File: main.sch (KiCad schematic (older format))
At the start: 27 parts, among them J4 Screw_Terminal_01x03, J5 Expansion, P1 TC2030-CTX-Tag-Connect-ESP32, U11 MAX485E, U12 TJA1051T, U13 TM8211, U2 ESP32-WROOM

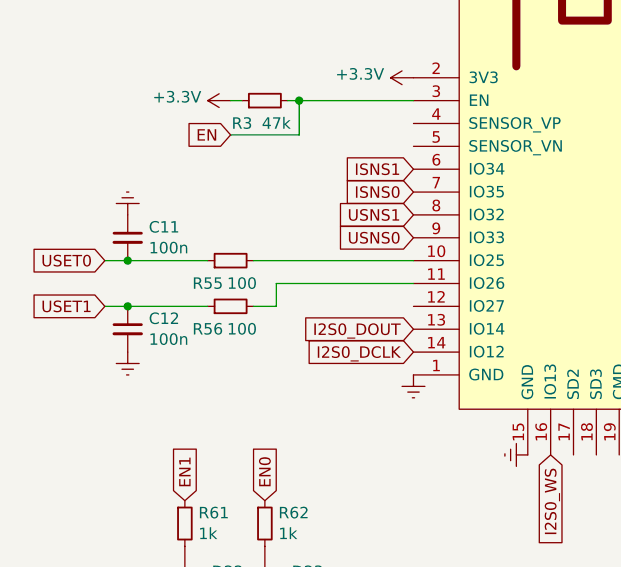
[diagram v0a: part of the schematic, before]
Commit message: modified Voltage DAC bias
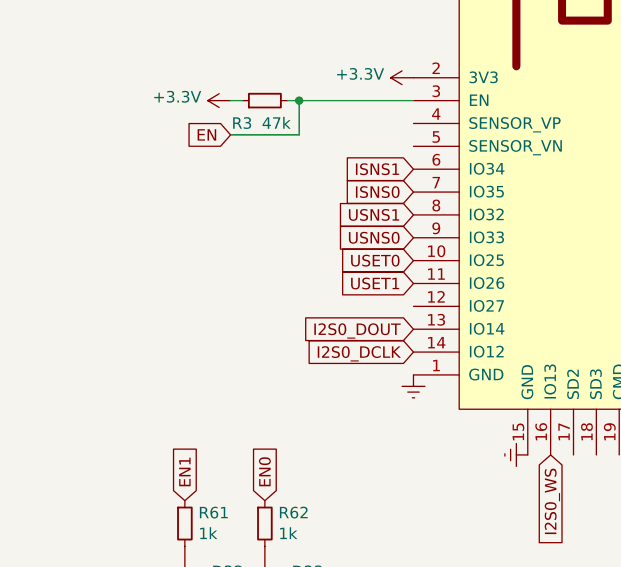
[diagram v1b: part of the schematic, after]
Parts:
- removed C11, C12: 100n, Capacitor_SMD:C_0603_1608Metric, symbol Device:C_Small
- removed R55, R56: 100, Resistor_SMD:R_0603_1608Metric, symbol Device:R_Small
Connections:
- net USET0: now also U2.10 (IO25)
- net USET1: now also U2.11 (IO26)
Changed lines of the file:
@@
 	0    1    1    0
 $EndComp
-$Comp
-L Device:R_Small R55
-U 1 1 5E938A76
-P 1550 2300
-F 0 "R55" V 1450 2400 50  0000 C CNN
-F 1 "100" V 1450 2250 50  0000 C CNN
-F 2 "Resistor_SMD:R_0603_1608Metric" H 1550 2300 50  0001 C CNN
-F 3 "~" H 1550 2300 50  0001 C CNN
-	1    1550 2300
-	0    -1   -1   0
-$EndComp
-$Comp
-L Device:R_Small R56
-U 1 1 5E938F12
-P 1550 2500
-F 0 "R56" V 1450 2600 50  0000 C CNN
-F 1 "100" V 1450 2450 50  0000 C CNN
-F 2 "Resistor_SMD:R_0603_1608Metric" H 1550 2500 50  0001 C CNN
-F 3 "~" H 1550 2500 50  0001 C CNN
-	1    1550 2500
-	0    -1   -1   0
-$EndComp
-Wire Wire Line
-	2350 2300 1650 2300
-Wire Wire Line
-	1650 2500 1750 2500
-Wire Wire Line
-	1750 2500 1750 2400
-Wire Wire Line
-	1750 2400 2350 2400
-$Comp
-L Device:C_Small C12
-U 1 1 5E93A3A4
-P 1100 2600
-F 0 "C12" H 1192 2646 50  0000 L CNN
-F 1 "100n" H 1192 2555 50  0000 L CNN
-F 2 "Capacitor_SMD:C_0603_1608Metric" H 1100 2600 50  0001 C CNN
-F 3 "~" H 1100 2600 50  0001 C CNN
-	1    1100 2600
-	1    0    0    -1
-$EndComp
-$Comp
-L Device:C_Small C11
-U 1 1 5E93AF9F
-P 1100 2200
-F 0 "C11" H 1192 2246 50  0000 L CNN
-F 1 "100n" H 1192 2155 50  0000 L CNN
-F 2 "Capacitor_SMD:C_0603_1608Metric" H 1100 2200 50  0001 C CNN
-F 3 "~" H 1100 2200 50  0001 C CNN
-	1    1100 2200
-	1    0    0    -1
-$EndComp
-$Comp
-L power:Earth #PWR0116
-U 1 1 5E93B328
-P 1100 2700
-F 0 "#PWR0116" H 1100 2450 50  0001 C CNN
-F 1 "Earth" H 1100 2550 50  0001 C CNN
-F 2 "" H 1100 2700 50  0001 C CNN
-F 3 "~" H 1100 2700 50  0001 C CNN
-	1    1100 2700
-	1    0    0    -1
-$EndComp
-$Comp
-L power:Earth #PWR0117
-U 1 1 5E93B608
-P 1100 2100
-F 0 "#PWR0117" H 1100 1850 50  0001 C CNN
-F 1 "Earth" H 1100 1950 50  0001 C CNN
-F 2 "" H 1100 2100 50  0001 C CNN
-F 3 "~" H 1100 2100 50  0001 C CNN
-	1    1100 2100
-	-1   0    0    1
-$EndComp
-Wire Wire Line
-	1100 2300 1450 2300
-Wire Wire Line
-	1450 2500 1100 2500
-Text GLabel 1000 2500 0    50   Input ~ 0
+Text GLabel 2350 2400 0    50   Input ~ 0
 USET1
-Text GLabel 1000 2300 0    50   Input ~ 0
+Text GLabel 2350 2300 0    50   Input ~ 0
 USET0
-Wire Wire Line
-	1000 2300 1100 2300
-Connection ~ 1100 2300
-Wire Wire Line
-	1100 2500 1000 2500
-Connection ~ 1100 2500
 Text GLabel 2950 3150 3    50   Input ~ 0
 I2S0_WS
